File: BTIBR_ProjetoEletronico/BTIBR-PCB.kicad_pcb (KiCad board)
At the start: 2 copper layers, 200 x 77 mm, 78 parts, among them J1 Screw_Terminal_01x03, J10 Screw_Terminal_01x03, J11 Conn_01x03_Male, J12 Screw_Terminal_01x03, J13 Conn_01x09_Male, J14 Screw_Terminal_01x04, J15 Conn_01x07_Male, J16 Screw_Terminal_01x03, J2 Conn_01x04_Male, J3 Conn_01x09_Male, J4 Screw_Terminal_01x04, J5 Conn_01x03_Male, J6 Screw_Terminal_01x03, J7 Conn_01x04_Male, J8 Conn_01x09_Male, J9 Screw_Terminal_01x04, U1 PC817, U10 PC817, U11 Module_X9C103S, U12 IC_LM331, U13 DRV8825, U2 Module_X9C103S, U3 IC_LM331, U4 DRV8825, U5 Module_LM2596, U6 PC817, U7 Module_X9C103S, U8 IC_LM331, U9 DRV8825

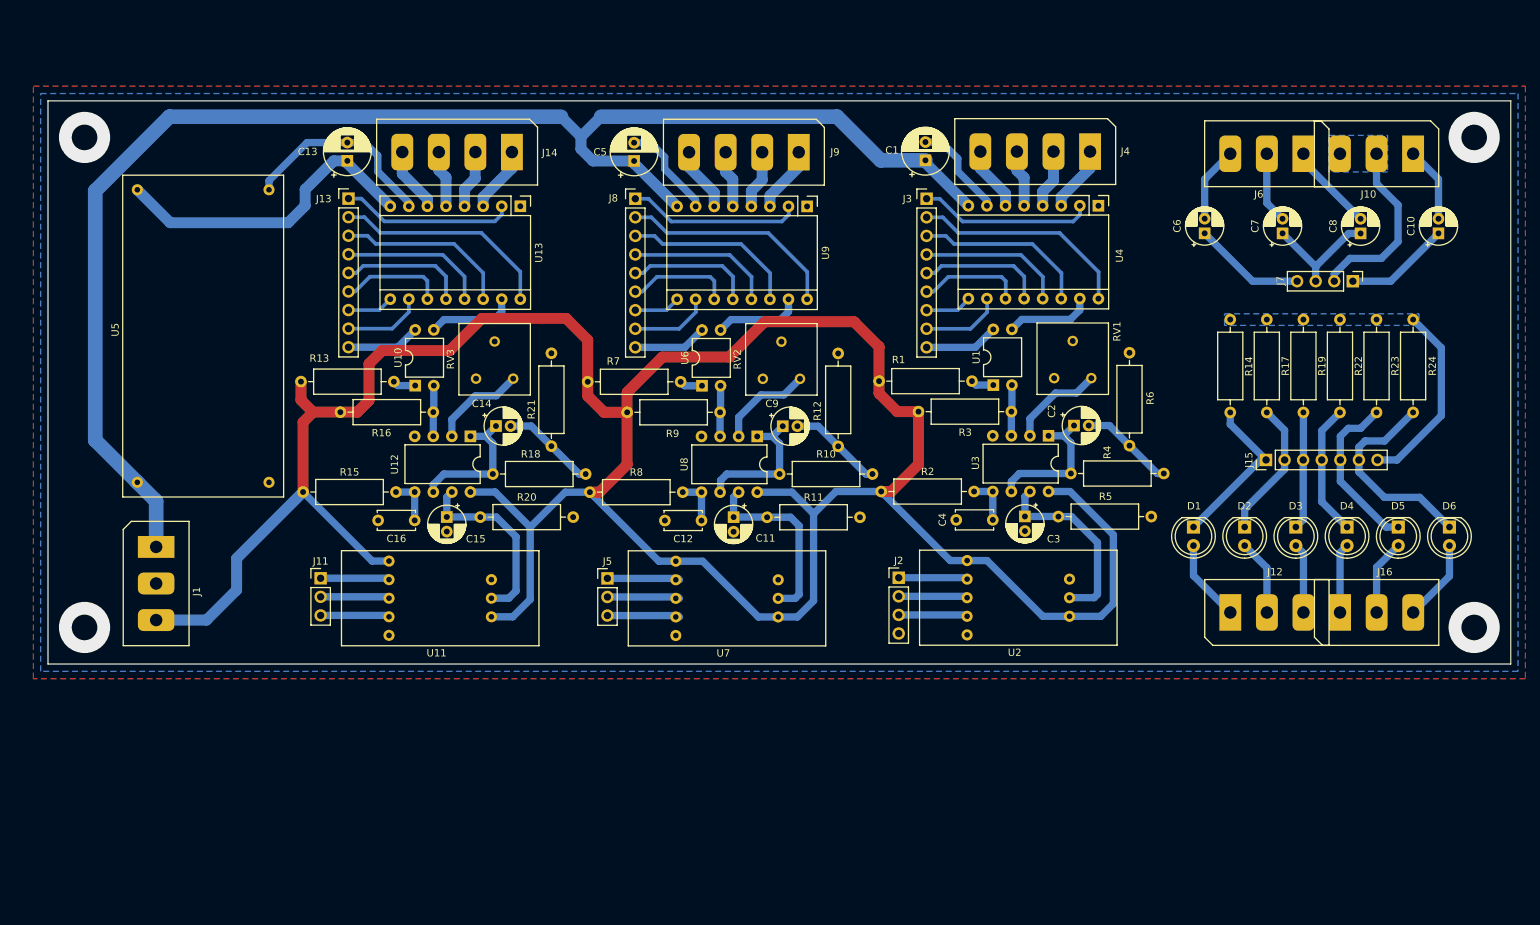
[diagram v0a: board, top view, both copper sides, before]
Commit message: Removido reglador de tensao da PCB
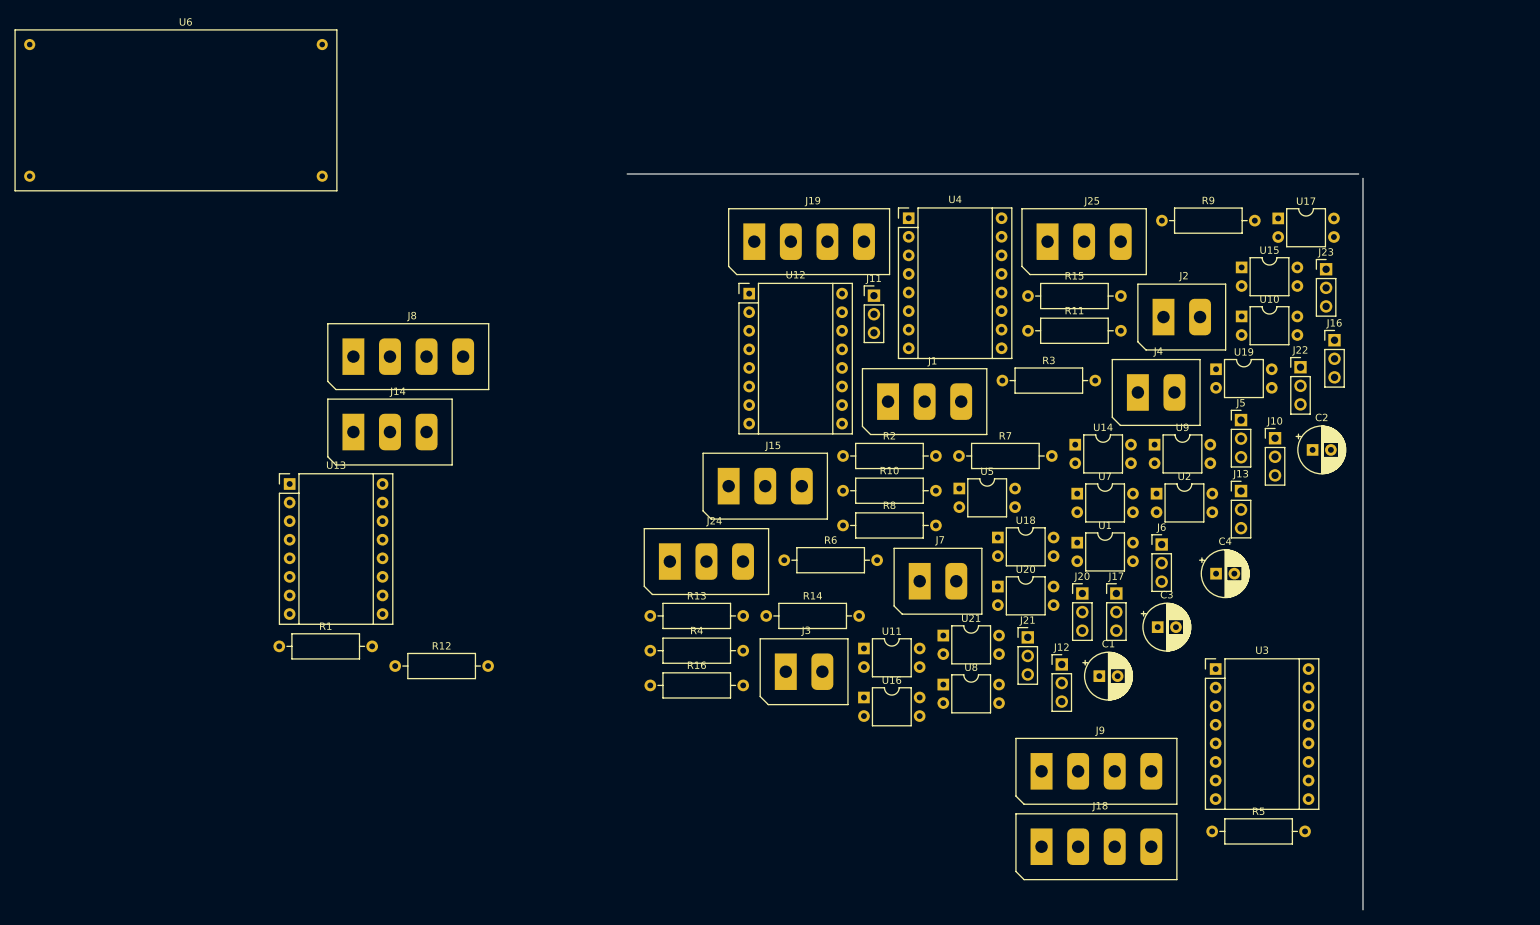
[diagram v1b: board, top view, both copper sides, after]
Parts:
- removed C10, C6, C7, C8: 10uF, Capacitor_THT:CP_Radial_D5.0mm_P2.00mm
- removed C11, C14, C15, C9: 1uF, Capacitor_THT:CP_Radial_D5.0mm_P2.00mm
- removed C12, C16: 10nF, Capacitor_THT:C_Disc_D5.0mm_W2.5mm_P5.00mm
- removed C13, C5: 100 μF, Capacitor_THT:CP_Radial_D6.3mm_P2.50mm
- removed D1, D2, D3, D4, D5, D6: LED, LED_THT:LED_D5.0mm
- removed R17, R19, R22, R23, R24: 1k, Resistor_THT:R_Axial_DIN0309_L9.0mm_D3.2mm_P12.70mm_Horizontal
- removed R18: 100k, Resistor_THT:R_Axial_DIN0309_L9.0mm_D3.2mm_P12.70mm_Horizontal
- removed R20: 2k7, Resistor_THT:R_Axial_DIN0309_L9.0mm_D3.2mm_P12.70mm_Horizontal
- removed R21: 47, Resistor_THT:R_Axial_DIN0309_L9.0mm_D3.2mm_P12.70mm_Horizontal
- removed RV1, RV2, RV3: 20k, FalcaroLib:Pot_3386F_Vertical
- added J17: Conn_01x03_Male, Connector_PinHeader_2.54mm:PinHeader_1x03_P2.54mm_Vertical, F.Cu at (196.1, 117.4)
- added J18: Screw_Terminal_01x04, FalcaroLib:Connector_Screw_4pin, F.Cu at (182.3, 147.5)
- added J19: Screw_Terminal_01x04, FalcaroLib:Connector_Screw_4pin, F.Cu at (143.1, 64.8)
- added J20: Conn_01x03_Male, Connector_PinHeader_2.54mm:PinHeader_1x03_P2.54mm_Vertical, F.Cu at (191.4, 117.4)
- added J21: Conn_01x03_Male, Connector_PinHeader_2.54mm:PinHeader_1x03_P2.54mm_Vertical, F.Cu at (184.0, 123.4)
- added J22: Conn_01x03_Male, Connector_PinHeader_2.54mm:PinHeader_1x03_P2.54mm_Vertical, F.Cu at (221.3, 86.4)
- added J23: Conn_01x03_Male, Connector_PinHeader_2.54mm:PinHeader_1x03_P2.54mm_Vertical, F.Cu at (224.8, 73.0)
- added J24: Screw_Terminal_01x03, FalcaroLib:Connector_Screw_3pin, F.Cu at (131.5, 108.5)
- added J25: Screw_Terminal_01x03, FalcaroLib:Connector_Screw_3pin, F.Cu at (183.2, 64.8)
- added U14: PC817, Package_DIP:DIP-4_W7.62mm, F.Cu at (190.5, 97.0)
- added U15: PC817, Package_DIP:DIP-4_W7.62mm, F.Cu at (213.2, 72.8)
- added U16: PC817, Package_DIP:DIP-4_W7.62mm, F.Cu at (161.6, 131.6)
- added U17: PC817, Package_DIP:DIP-4_W7.62mm, F.Cu at (218.2, 66.1)
- added U18: PC817, Package_DIP:DIP-4_W7.62mm, F.Cu at (179.9, 109.7)
- added U19: PC817, Package_DIP:DIP-4_W7.62mm, F.Cu at (209.7, 86.7)
- added U20: PC817, Package_DIP:DIP-4_W7.62mm, F.Cu at (179.9, 116.4)
- added U21: PC817, Package_DIP:DIP-4_W7.62mm, F.Cu at (172.4, 123.1)
- C2, C3: value 1uF -> 100 μF; footprint Capacitor_THT:CP_Radial_D5.0mm_P2.00mm -> Capacitor_THT:CP_Radial_D6.3mm_P2.50mm
- C4: value 10nF -> 100 μF; footprint Capacitor_THT:C_Disc_D5.0mm_W2.5mm_P5.00mm -> Capacitor_THT:CP_Radial_D6.3mm_P2.50mm
- J10, J12, J16, J6: value Screw_Terminal_01x03 -> Conn_01x03_Male; footprint FalcaroLib:Connector_Screw_3pin -> Connector_PinHeader_2.54mm:PinHeader_1x03_P2.54mm_Vertical
- J13: value Conn_01x09_Male -> Conn_01x03_Male; footprint Connector_PinHeader_2.54mm:PinHeader_1x09_P2.54mm_Vertical -> Connector_PinHeader_2.54mm:PinHeader_1x03_P2.54mm_Vertical
- J14: value Screw_Terminal_01x04 -> Screw_Terminal_01x03; footprint FalcaroLib:Connector_Screw_4pin -> FalcaroLib:Connector_Screw_3pin
- J15: value Conn_01x07_Male -> Screw_Terminal_01x03; footprint Connector_PinHeader_2.54mm:PinHeader_1x07_P2.54mm_Vertical -> FalcaroLib:Connector_Screw_3pin
- J2, J7: value Conn_01x04_Male -> Screw_Terminal_01x02; footprint Connector_PinHeader_2.54mm:PinHeader_1x04_P2.54mm_Vertical -> FalcaroLib:Connector_Screw_2pin
- J3: value Conn_01x09_Male -> Screw_Terminal_01x02; footprint Connector_PinHeader_2.54mm:PinHeader_1x09_P2.54mm_Vertical -> FalcaroLib:Connector_Screw_2pin
- J4: value Screw_Terminal_01x04 -> Screw_Terminal_01x02; footprint FalcaroLib:Connector_Screw_4pin -> FalcaroLib:Connector_Screw_2pin
- J8: value Conn_01x09_Male -> Screw_Terminal_01x04; footprint Connector_PinHeader_2.54mm:PinHeader_1x09_P2.54mm_Vertical -> FalcaroLib:Connector_Screw_4pin
- R1, R13, R7: value 220 -> 1k
- R10, R4: value 100k -> 1k
- R11, R5: value 2k7 -> 1k
- R12, R6: value 47 -> 1k
- R15, R2, R8: value 5k6 -> 1k
- R16, R3, R9: value 10k -> 1k
- U11, U2, U7: value Module_X9C103S -> PC817; footprint FalcaroLib:Module_X9C103S -> Package_DIP:DIP-4_W7.62mm
- U12, U3: value IC_LM331 -> DRV8825; footprint Package_DIP:DIP-8_W7.62mm -> FalcaroLib:Module_DRV8825
- U5: value Module_LM2596 -> PC817; footprint FalcaroLib:Module_LM2596 -> Package_DIP:DIP-4_W7.62mm
- U6: value PC817 -> Module_LM2596; footprint Package_DIP:DIP-4_W7.62mm -> FalcaroLib:Module_LM2596
- U8: value IC_LM331 -> PC817; footprint Package_DIP:DIP-8_W7.62mm -> Package_DIP:DIP-4_W7.62mm
- U9: value DRV8825 -> PC817; footprint FalcaroLib:Module_DRV8825 -> Package_DIP:DIP-4_W7.62mm
- moved J13 128.4 mm to (213.1, 103.3)
- moved U10 113.4 mm to (213.2, 79.5), turned to 0 degrees
- moved U5 112.4 mm to (174.6, 103.0), turned to 0 degrees
- moved U6 103.1 mm to (47.5, 42.3), turned to 0 degrees
- moved R15 102.7 mm to (184.0, 76.7)
- moved R1 101.4 mm to (81.6, 124.6), turned to 0 degrees
- moved J1 94.4 mm to (161.4, 86.6), turned to 0 degrees
- moved J5 89.3 mm to (213.1, 93.6)
- moved J11 84.9 mm to (162.9, 76.6)
- moved J9 80.1 mm to (182.3, 137.2), turned to 0 degrees
- moved R9 77.7 mm to (202.3, 66.4)
- moved J15 77.0 mm to (139.6, 98.2), turned to 0 degrees
- moved R14 75.3 mm to (148.2, 120.4), turned to 0 degrees
- moved C1 74.4 mm to (193.8, 128.7), turned to 0 degrees
- moved J7 72.6 mm to (165.7, 111.2), turned to 0 degrees
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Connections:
- C2 pad 1: Net-(C2-Pad1) -> +12V
- C2 pad 2: Net-(C2-Pad2) -> GND
- C3 pad 1: Net-(C3-Pad1) -> +12V
- C4 pad 1: Net-(C4-Pad1) -> +8V
- C4 pad 2: GND -> GND1
- J10 pad 1: Net-(C10-Pad2) -> +5V
- J10 pad 2: Net-(J10-Pad2) -> M1_M1
- J10 pad 3: Net-(J10-Pad2) -> GND
- J11 pad 1: Net-(J11-Pad1) -> +5V
- J11 pad 2: Net-(J11-Pad2) -> M2_M1
- J11 pad 3: Net-(J11-Pad3) -> GND
- J12 pad 1: Net-(D1-Pad2) -> +5V
- J12 pad 2: Net-(D2-Pad2) -> M1_M2
- J12 pad 3: Net-(D3-Pad2) -> GND
- J13 pad 1: Net-(J13-Pad1) -> +5V
- J13 pad 2: Net-(J13-Pad2) -> M2_M2
- J13 pad 3: Net-(J13-Pad3) -> GND
- J15 pad 1: FDC1 -> Net-(J15-Pad1)
- J15 pad 2: FDC2 -> Net-(J15-Pad2)
- J15 pad 3: FDC3 -> Net-(J15-Pad3)
- J16 pad 1: Net-(D4-Pad2) -> +5V
- J16 pad 2: Net-(D5-Pad2) -> M3_M0
- J16 pad 3: Net-(D6-Pad2) -> GND
- J5 pad 1: Net-(J5-Pad1) -> +5V
- J5 pad 2: Net-(J5-Pad2) -> M1_M0
- J5 pad 3: Net-(J5-Pad3) -> GND
- J6 pad 1: Net-(C8-Pad2) -> +5V
- J6 pad 2: Net-(C7-Pad2) -> M2_M0
- J6 pad 3: Net-(C6-Pad2) -> GND
- J7 pad 1: Net-(C10-Pad1) -> Net-(J7-Pad1)
- J7 pad 2: Net-(J10-Pad2) -> Net-(J7-Pad2)
- R1 pad 2: +5V -> Net-(J2-Pad1)
- R10 pad 1: Net-(C9-Pad1) -> Net-(R10-Pad1)
- R10 pad 2: Net-(C9-Pad2) -> Net-(J15-Pad1)
- R11 pad 1: Net-(C11-Pad1) -> Net-(R11-Pad1)
- R11 pad 2: GND -> Net-(J24-Pad3)
- R12 pad 1: Net-(C9-Pad2) -> Net-(R12-Pad1)
- R12 pad 2: GND -> Net-(J25-Pad3)
- R13 pad 2: +5V -> Net-(J24-Pad2)
- R14 pad 1: FDC-GND -> Net-(R14-Pad1)
- R14 pad 2: FDC1 -> Net-(J25-Pad2)
- R15 pad 1: +5V -> Net-(R15-Pad1)
- R15 pad 2: Net-(C16-Pad1) -> Net-(J24-Pad1)
- R16 pad 1: +5V -> Net-(R16-Pad1)
- R16 pad 2: Net-(R16-Pad2) -> Net-(J25-Pad1)
- R2 pad 1: +5V -> Net-(R2-Pad1)
- R2 pad 2: Net-(C4-Pad1) -> Net-(J2-Pad2)
- R3 pad 1: +5V -> Net-(R3-Pad1)
- R3 pad 2: Net-(R3-Pad2) -> Net-(J3-Pad1)
- R4 pad 1: Net-(C2-Pad1) -> Net-(R4-Pad1)
- R4 pad 2: Net-(C2-Pad2) -> Net-(J3-Pad2)
- R5 pad 1: Net-(C3-Pad1) -> Net-(R5-Pad1)
- R5 pad 2: GND -> Net-(J14-Pad3)
- R6 pad 1: Net-(C2-Pad2) -> Net-(R6-Pad1)
- R6 pad 2: GND -> Net-(J15-Pad3)
- R7 pad 2: +5V -> Net-(J14-Pad2)
- R8 pad 1: +5V -> Net-(R8-Pad1)
- R8 pad 2: Net-(C12-Pad1) -> Net-(J15-Pad2)
- R9 pad 1: +5V -> Net-(R9-Pad1)
- R9 pad 2: Net-(R9-Pad2) -> Net-(J14-Pad1)
- U1 pad 2: Net-(R3-Pad2) -> GND
- U1 pad 3: M1_CLK -> Net-(J4-Pad1)
- U1 pad 4: M1_STEP -> +5V
- U10 pad 1: Net-(R13-Pad1) -> Net-(R7-Pad1)
- U10 pad 2: Net-(R16-Pad2) -> GND
- U10 pad 3: M3_CLK -> M1_STEP
- U10 pad 4: M3_STEP -> +5V
- U11 pad 1: +5V -> Net-(R8-Pad1)
- U11 pad 2: Net-(J11-Pad1) -> GND
- U11 pad 3: Net-(J11-Pad2) -> M2_STEP
- U11 pad 4: Net-(J11-Pad3) -> +5V
- U12 pad 1: Net-(C14-Pad1) -> GND
- U12 pad 3: Net-(R16-Pad2) -> Net-(J18-Pad1)
- U12 pad 4: GND -> Net-(J18-Pad2)
- U12 pad 5: Net-(C16-Pad1) -> Net-(J18-Pad3)
- U12 pad 6: Net-(C14-Pad1) -> Net-(J18-Pad4)
- U12 pad 7: Net-(C15-Pad1) -> GND1
- U12 pad 8: +5V -> +8V
- U13 pad 10: Net-(J13-Pad8) -> M8_M0
- U13 pad 11: Net-(J13-Pad6) -> M8_M1
- U13 pad 12: Net-(J13-Pad5) -> M8_M2
- U13 pad 13: Net-(J13-Pad4) -> +5V
- U13 pad 14: Net-(J13-Pad3) -> +5V
- U13 pad 15: M3_CLK -> M8_STEP
- U13 pad 16: Net-(J13-Pad2) -> M8_DIR
- U13 pad 2: Net-(J13-Pad1) -> Net-(U13-Pad2)
- U13 pad 3: Net-(J14-Pad1) -> Net-(J19-Pad1)
- U13 pad 4: Net-(J14-Pad2) -> Net-(J19-Pad2)
- U13 pad 5: Net-(J14-Pad3) -> Net-(J19-Pad3)
- U13 pad 6: Net-(J14-Pad4) -> Net-(J19-Pad4)
- U13 pad 7: GND1 -> GND
- U13 pad 8: +8V -> +12V
- U13 pad 9: Net-(J13-Pad7) -> M8_EN
- U2 pad 1: +5V -> Net-(R2-Pad1)
- U2 pad 2: Net-(J2-Pad1) -> GND
- U2 pad 3: Net-(J2-Pad2) -> Net-(J4-Pad2)
- U2 pad 4: Net-(J2-Pad3) -> +5V
- U3 pad 1: Net-(C2-Pad1) -> GND
- U3 pad 3: Net-(R3-Pad2) -> Net-(J8-Pad1)
- U3 pad 4: GND -> Net-(J8-Pad2)
- U3 pad 5: Net-(C4-Pad1) -> Net-(J8-Pad3)
- U3 pad 6: Net-(C2-Pad1) -> Net-(J8-Pad4)
- U3 pad 7: Net-(C3-Pad1) -> GND
- U3 pad 8: +5V -> +12V
- U4 pad 10: Net-(J3-Pad8) -> M2_M0
- U4 pad 11: Net-(J3-Pad6) -> M2_M1
- U4 pad 12: Net-(J3-Pad5) -> M2_M2
- U4 pad 13: Net-(J3-Pad4) -> +5V
- U4 pad 14: Net-(J3-Pad3) -> +5V
- U4 pad 15: M1_CLK -> M2_STEP
- U4 pad 16: Net-(J3-Pad2) -> M2_DIR
- U4 pad 2: Net-(J3-Pad1) -> Net-(U4-Pad2)
- U4 pad 3: Net-(J4-Pad1) -> Net-(J9-Pad1)
- U4 pad 4: Net-(J4-Pad2) -> Net-(J9-Pad2)
- U4 pad 5: Net-(J4-Pad3) -> Net-(J9-Pad3)
- U4 pad 6: Net-(J4-Pad4) -> Net-(J9-Pad4)
- U4 pad 9: Net-(J3-Pad7) -> M2_EN
- U7 pad 1: +5V -> Net-(R4-Pad1)
- U7 pad 2: Net-(J5-Pad1) -> GND
- U7 pad 3: Net-(J5-Pad2) -> Net-(J7-Pad2)
- U7 pad 4: Net-(J5-Pad3) -> +5V
- U8 pad 1: Net-(C9-Pad1) -> Net-(R5-Pad1)
- U8 pad 2: Net-(RV2-Pad1) -> GND
- U8 pad 3: Net-(R9-Pad2) -> M1_EN
- U8 pad 4: GND -> +5V
- U9 pad 1: GND -> Net-(R6-Pad1)
- U9 pad 2: Net-(J8-Pad1) -> GND
- U9 pad 3: Net-(J9-Pad1) -> M2_EN
- U9 pad 4: Net-(J9-Pad2) -> +5V
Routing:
- net +5V: track 372.5 -> 0.00 mm
- net +12V: track 201.5 -> 0.00 mm
- net +8V: track 44.0 -> 0.00 mm
- net Net-(J3-Pad2): track 30.3 -> 0.00 mm
- net Net-(J13-Pad2): track 30.3 -> 0.00 mm
- net Net-(J8-Pad2): track 30.3 -> 0.00 mm
- net FDC6: track 28.3 -> 0.00 mm
- net GND1: track 27.7 -> 0.00 mm
- net GND: track 27.0 -> 0.00 mm
- net Net-(C3-Pad1): track 26.2 -> 0.00 mm
- net FDC-GND: track 26.0 -> 0.00 mm
- net Net-(C11-Pad1): track 25.6 -> 0.00 mm
- net Net-(C15-Pad1): track 25.5 -> 0.00 mm
- net Net-(J10-Pad2): track 24.8 -> 0.00 mm
- net Net-(J8-Pad3): track 24.1 -> 0.00 mm
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- removed copper zone on B.Cu, net FDC-GND
- removed copper zone on B.Cu, net GND
- removed copper zone on F.Cu, net GND
- removed copper zone on B.Cu, net Net-(J10-Pad2)
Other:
- board size 200 x 77 mm -> 100.6 x 100.6 mm

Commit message: Finalizado desenvolvimento da PCB
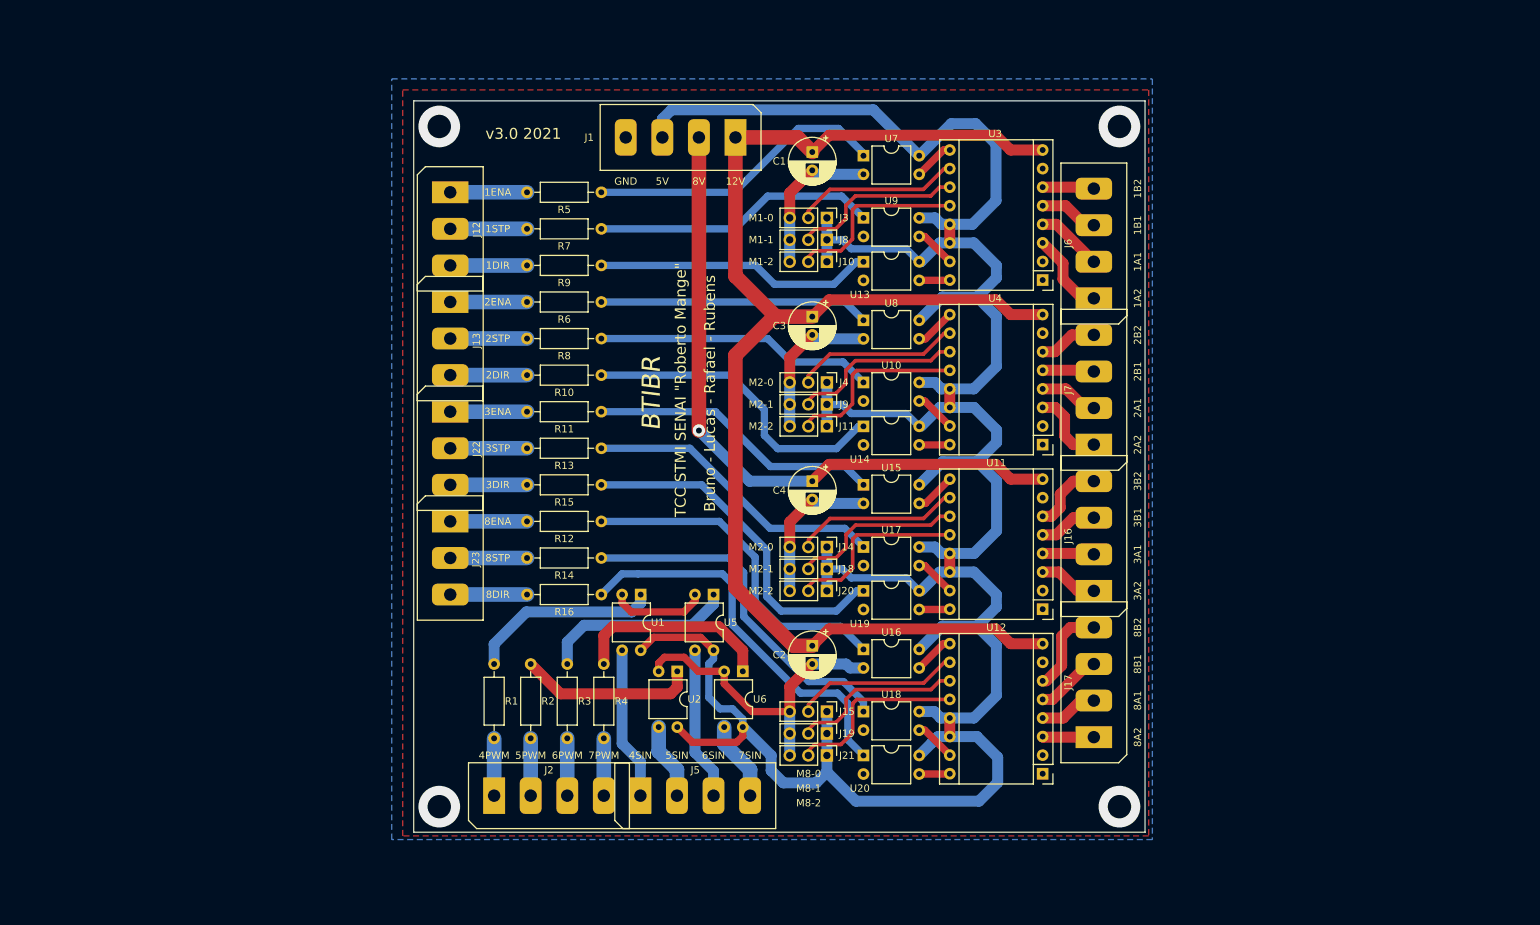
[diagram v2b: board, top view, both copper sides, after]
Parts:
- removed the J12 at (188.6, 127.1)
- removed the J13 at (213.1, 103.3)
- removed the J16 at (225.9, 82.7)
- removed the J17 at (196.1, 117.4)
- removed the J22 at (221.3, 86.4)
- removed the J23 at (224.8, 73.0)
- removed the J6 at (202.3, 110.7)
- removed the J7 at (165.7, 111.2)
- removed the U12 at (145.9, 76.4)
- removed the U6 at (47.5, 42.3)
- removed the U8 at (172.4, 129.8)
- added J14: Conn_01x03_Male, Connector_PinHeader_2.54mm:PinHeader_1x03_P2.54mm_Vertical, F.Cu at (156.5, 111.0)
- added J15: Conn_01x03_Male, Connector_PinHeader_2.54mm:PinHeader_1x03_P2.54mm_Vertical, F.Cu at (156.5, 133.5)
- added J18: Conn_01x03_Male, Connector_PinHeader_2.54mm:PinHeader_1x03_P2.54mm_Vertical, F.Cu at (156.5, 114.0)
- added J19: Conn_01x03_Male, Connector_PinHeader_2.54mm:PinHeader_1x03_P2.54mm_Vertical, F.Cu at (156.5, 136.5)
- added J8: Conn_01x03_Male, Connector_PinHeader_2.54mm:PinHeader_1x03_P2.54mm_Vertical, F.Cu at (156.5, 69.0)
- added J9: Conn_01x03_Male, Connector_PinHeader_2.54mm:PinHeader_1x03_P2.54mm_Vertical, F.Cu at (156.5, 91.5)
- added U11: DRV8825, FalcaroLib:Module_DRV8825, F.Cu at (186.0, 119.5)
- added U7: PC817, Package_DIP:DIP-4_W7.62mm, F.Cu at (161.5, 57.5)
- J1: value Screw_Terminal_01x03 -> Screw_Terminal_01x04; footprint FalcaroLib:Connector_Screw_3pin -> FalcaroLib:Connector_Screw_4pin
- J2: value Screw_Terminal_01x02 -> Screw_Terminal_01x04; footprint FalcaroLib:Connector_Screw_2pin -> FalcaroLib:Connector_Screw_4pin
- J3, J4: value Screw_Terminal_01x02 -> Conn_01x03_Male; footprint FalcaroLib:Connector_Screw_2pin -> Connector_PinHeader_2.54mm:PinHeader_1x03_P2.54mm_Vertical
- J5: value Conn_01x03_Male -> Screw_Terminal_01x04; footprint Connector_PinHeader_2.54mm:PinHeader_1x03_P2.54mm_Vertical -> FalcaroLib:Connector_Screw_4pin
- R1, R10, R11, R12, R13, R14, R15, R16, R2, R3, R4, R5, R6, R7, R8, R9: footprint Resistor_THT:R_Axial_DIN0309_L9.0mm_D3.2mm_P12.70mm_Horizontal -> Resistor_THT:R_Axial_DIN0207_L6.3mm_D2.5mm_P10.16mm_Horizontal
- moved R5 120.9 mm to (125.7, 62.5), turned to 180 degrees
- moved J2 112.5 mm to (107.5, 140.5)
- moved U12 110.3 mm to (186.0, 142.0), turned to 180 degrees
- moved J6 100.2 mm to (188.5, 80.5), turned to 90 degrees
- moved J5 97.6 mm to (127.5, 140.5)
- moved J17 88.3 mm to (188.5, 140.5), turned to 90 degrees
- moved J23 83.5 mm to (109.5, 104.0), turned to 270 degrees
- moved U16 81.8 mm to (161.5, 125.0)
- moved C1 81.7 mm to (154.5, 57.0), turned to 270 degrees
- moved R9 76.9 mm to (125.7, 72.5), turned to 180 degrees
- moved C2 73.5 mm to (154.5, 124.5), turned to 270 degrees
- moved R3 71.0 mm to (121.0, 127.0), turned to 270 degrees
- moved U2 69.9 mm to (136.0, 128.0), turned to 270 degrees
- moved U18 67.2 mm to (161.5, 133.5)
- moved J10 65.9 mm to (156.5, 72.0), turned to 270 degrees
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- renumbered J14 to J12, J15 to J13, J18 to J16, J19 to J17, J24 to J22, J25 to J23, J8 to J6, J9 to J7, U11 to U10, U13 to U12, U14 to U13, U15 to U14, U16 to U15, U17 to U16, U18 to U17, U19 to U18, U20 to U19, U21 to U20, U7 to U6, U9 to U8, U10 to U9
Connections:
- C4 pad 2: GND1 -> GND
- J1 pad 2: GND -> +8V
- J10 pad 2: M1_M1 -> M1_M2
- J11 pad 2: M2_M1 -> M2_M2
- J12 pad 1: Net-(J14-Pad1) -> Net-(J12-Pad1)
- J12 pad 3: Net-(J14-Pad3) -> Net-(J12-Pad3)
- J13 pad 1: Net-(J15-Pad1) -> Net-(J13-Pad1)
- J13 pad 3: Net-(J15-Pad3) -> Net-(J13-Pad3)
- J20 pad 2: M3_M1 -> M3_M2
- J21 pad 2: M8_M1 -> M8_M2
- J22 pad 1: Net-(J24-Pad1) -> Net-(J22-Pad1)
- J22 pad 3: Net-(J24-Pad3) -> Net-(J22-Pad3)
- J23 pad 1: Net-(J25-Pad1) -> Net-(J23-Pad1)
- J23 pad 3: Net-(J25-Pad3) -> Net-(J23-Pad3)
- J3 pad 1: Net-(J3-Pad1) -> +5V
- J3 pad 2: Net-(J3-Pad2) -> M1_M0
- J4 pad 1: Net-(J4-Pad1) -> +5V
- J4 pad 2: Net-(J4-Pad2) -> M2_M0
- J5 pad 1: +5V -> Net-(J5-Pad1)
- J5 pad 2: M1_M0 -> Net-(J5-Pad2)
- J5 pad 3: GND -> Net-(J5-Pad3)
- R10 pad 2: Net-(J15-Pad1) -> Net-(J13-Pad3)
- R11 pad 2: Net-(J24-Pad3) -> Net-(J22-Pad1)
- R12 pad 2: Net-(J25-Pad3) -> Net-(J23-Pad1)
- R15 pad 2: Net-(J24-Pad1) -> Net-(J22-Pad3)
- R16 pad 2: Net-(J25-Pad1) -> Net-(J23-Pad3)
- R3 pad 2: Net-(J3-Pad1) -> Net-(J2-Pad3)
- R4 pad 2: Net-(J3-Pad2) -> Net-(J2-Pad4)
- R5 pad 2: Net-(J14-Pad3) -> Net-(J12-Pad1)
- R6 pad 2: Net-(J15-Pad3) -> Net-(J13-Pad1)
- R9 pad 2: Net-(J14-Pad1) -> Net-(J12-Pad3)
- U1 pad 3: Net-(J4-Pad1) -> Net-(J5-Pad1)
- U2 pad 3: Net-(J4-Pad2) -> Net-(J5-Pad2)
- U5 pad 3: Net-(J7-Pad1) (its old number) -> Net-(J5-Pad3)
- U6 pad 3: Net-(J7-Pad2) (its old number) -> Net-(J5-Pad4)
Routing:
- net +5V: track 0.00 -> 398.2 mm
- net +12V: track 0.00 -> 196.2 mm
- net GND: track 0.00 -> 120.5 mm
- net +8V: track 0.00 -> 91.7 mm, vias 0 -> 1
- net Net-(R16-Pad1): track 0.00 -> 53.5 mm
- net Net-(R14-Pad1): track 0.00 -> 48.8 mm
- net Net-(R15-Pad1): track 0.00 -> 47.9 mm
- net Net-(R12-Pad1): track 0.00 -> 46.6 mm
- net Net-(R10-Pad1): track 0.00 -> 43.3 mm
- net Net-(R13-Pad1): track 0.00 -> 41.4 mm
- net Net-(R5-Pad1): track 0.00 -> 41.2 mm
- net Net-(R11-Pad1): track 0.00 -> 40.0 mm
- net Net-(R7-Pad1): track 0.00 -> 38.9 mm
- net Net-(R8-Pad1): track 0.00 -> 38.3 mm
- net Net-(R9-Pad1): track 0.00 -> 38.2 mm
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- added copper zone on B.Cu, net GND
- added copper zone on F.Cu, net GND
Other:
- board size 100.6 x 100.6 mm -> 100 x 100 mm
- board text added: "12V"
- board text added: "1A1"
- board text added: "1A2"
- board text added: "1B1"
- board text added: "1B2"
- board text added: "1DIR"
- board text added: "1ENA"
- board text added: "1STP"
- board text added: "2A1"
- board text added: "2A2"
- board text added: "2B1"
- board text added: "2B2"
- board text added: "2DIR"
- board text added: "2ENA"
- board text added: "2STP"
- board text added: "3A1"
- board text added: "3A2"
- board text added: "3B1"
- board text added: "3B2"
- board text added: "3DIR"
- board text added: "3ENA"
- board text added: "3STP"
- board text added: "4PWM"
- board text added: "4SIN"
- board text added: "5PWM"
- board text added: "5SIN"
- board text added: "5V"
- board text added: "6PWM"
- board text added: "6SIN"
- board text added: "7PWM"
- board text added: "7SIN"
- board text added: "8A1"
- board text added: "8A2"
- board text added: "8B1"
- board text added: "8B2"
- board text added: "8DIR"
- board text added: "8ENA"
- board text added: "8STP"
- board text added: "8V"
- board text added: "BTIBR"
- board text added: "Bruno - Lucas - Rafael - Rubens"
- board text added: "GND"
- board text added: "M1-0"
- board text added: "M1-1"
- board text added: "M1-2"
- board text added: "M2-0"
- board text added: "M2-1"
- board text added: "M2-2"
- board text added: "M8-0"
- board text added: "M8-1"
- board text added: "M8-2"
- board text added: "TCC STMI SENAI "Roberto Mange""
- board text added: "v3.0 2021"
